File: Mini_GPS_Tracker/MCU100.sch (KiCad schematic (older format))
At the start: 12 parts

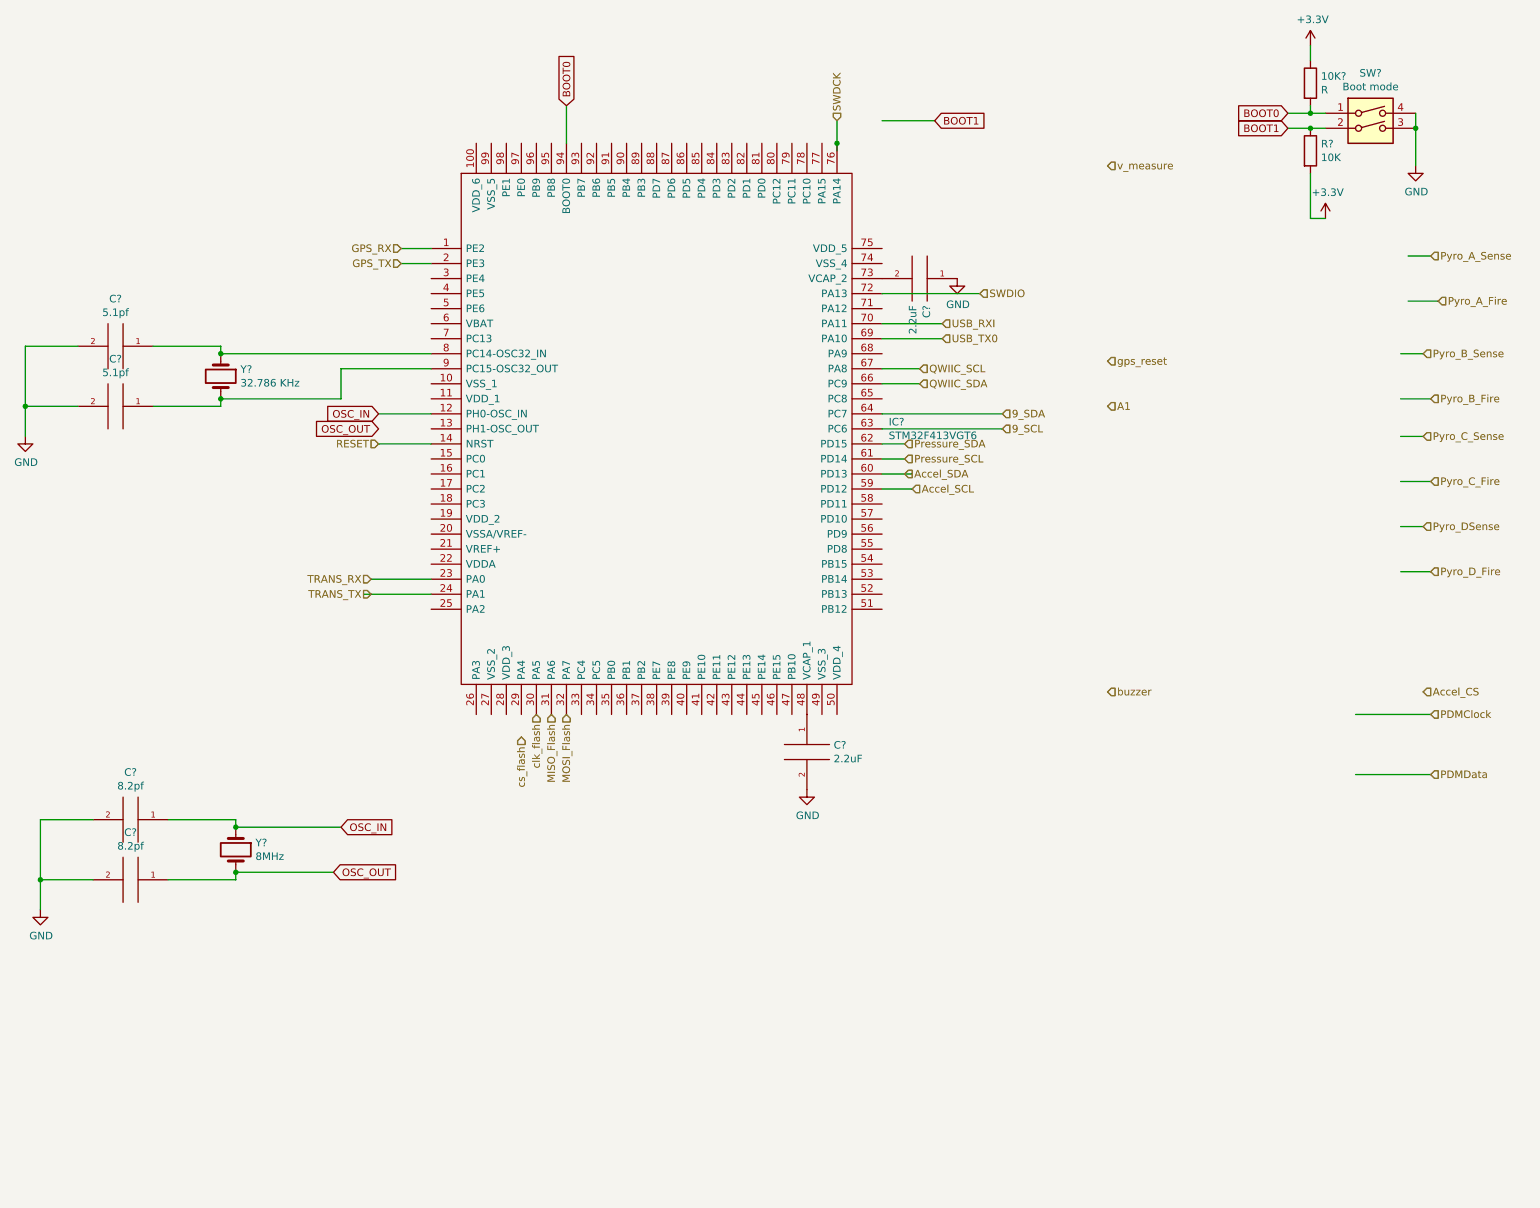
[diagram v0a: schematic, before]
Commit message: Add files via upload
Making update for 100 pin CPU
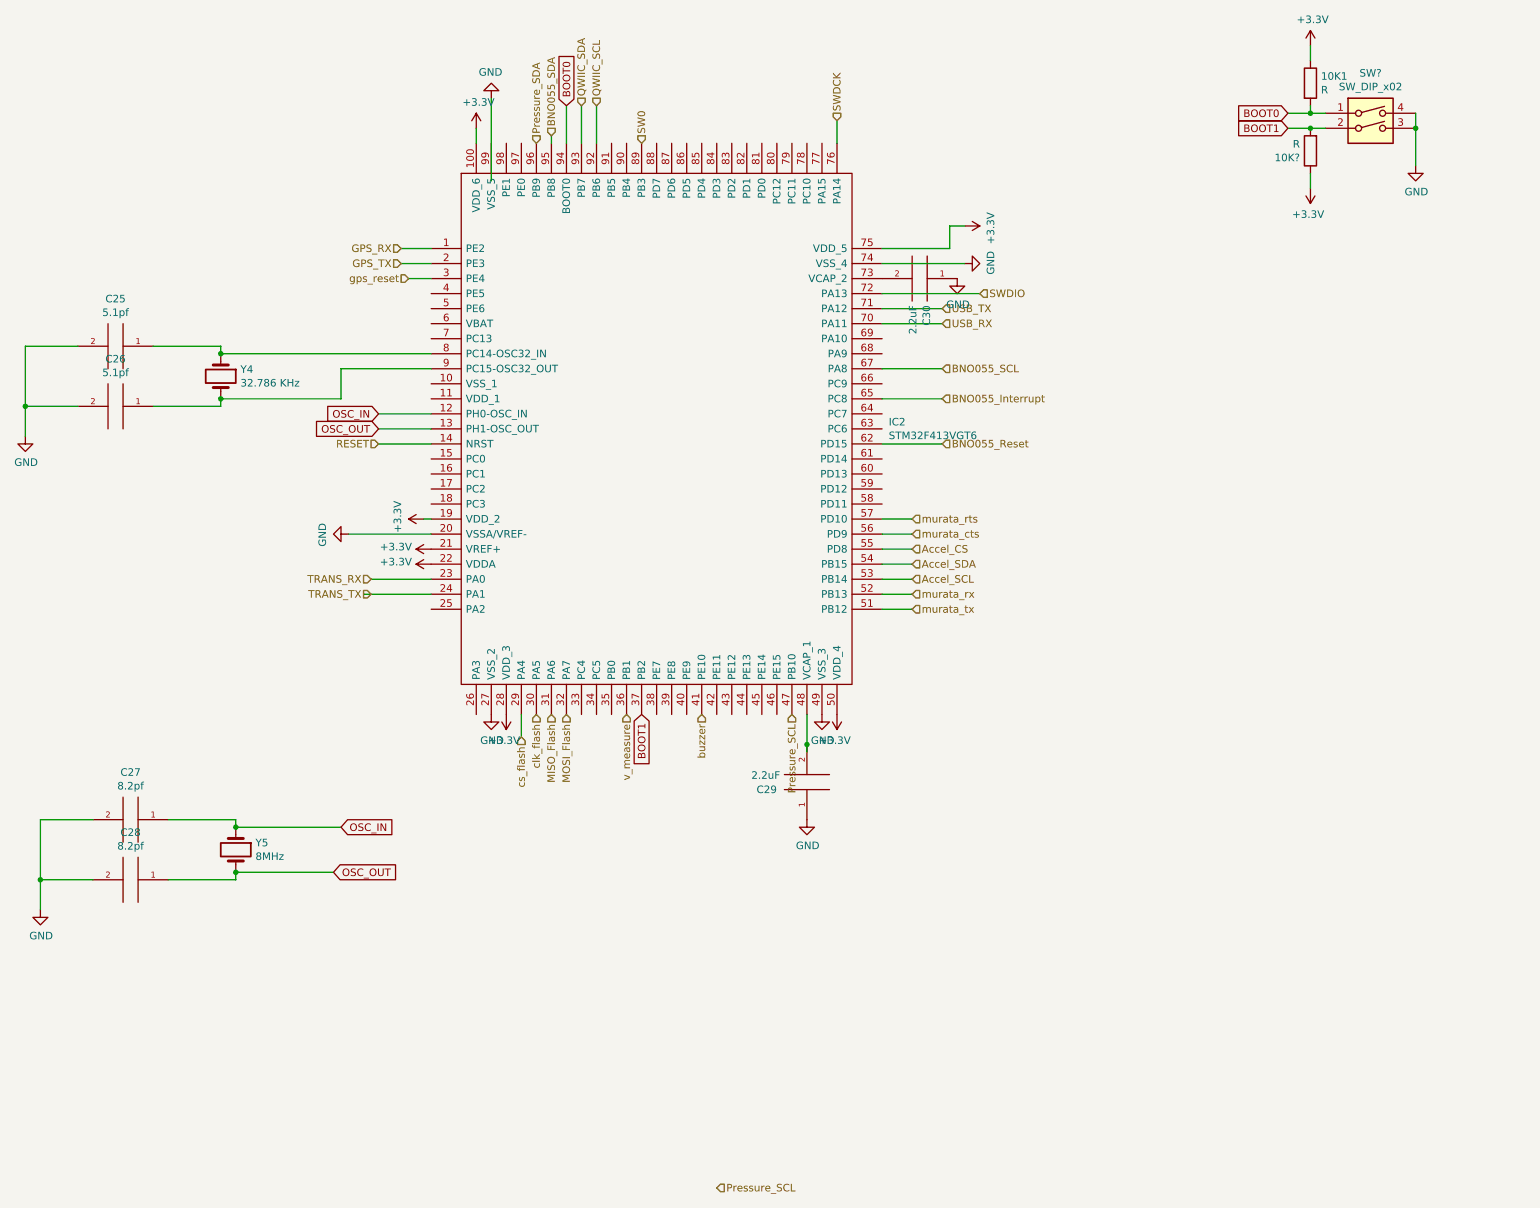
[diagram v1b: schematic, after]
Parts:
- removed R?: 10K, symbol Device:R
- removed SW?: Boot mode, symbol Switch:SW_DIP_x02
- added 10K?: R, symbol Device:R
- added SW?: SW_DIP_x02, symbol Switch:SW_DIP_x02
- gave numbers to parts that had none: 10
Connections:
- net labels added: BNO055_Interrupt, BNO055_Reset, BNO055_SCL, BNO055_SDA, SW0, USB_RX, USB_TX, murata_cts, murata_rts, murata_rx, murata_tx
- net labels removed: 9_SCL, 9_SDA, A1, PDMClock, PDMData, Pyro_A_Fire, Pyro_A_Sense, Pyro_B_Fire, Pyro_B_Sense, Pyro_C_Fire, Pyro_C_Sense, Pyro_DSense, Pyro_D_Fire, USB_RXI, USB_TX0
- wire segments 63 -> 68
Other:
- moved on the sheet: C29

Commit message: Add files via upload
Splitting board into modules
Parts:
- gave numbers to parts that had none: 2
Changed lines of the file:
@@
 $Descr A4 11693 8268
 encoding utf-8
-Sheet 7 7
+Sheet 7 13
 Title ""
 Date ""
@@
 P 9550 1950
 AR Path="/5E9FE63A/5EAF1BAE" Ref="10K?"  Part="1"
-AR Path="/5EA0B5A0/5EAF1BAE" Ref="10K?"  Part="1"
-F 0 "10K?" H 9620 1996 50  0000 L CNN
+AR Path="/5EA0B5A0/5EAF1BAE" Ref="10K2"  Part="1"
+F 0 "10K2" H 9620 1996 50  0000 L CNN
 F 1 "R" H 9620 1905 50  0000 L CNN
 F 2 "" V 9480 1950 50  0001 C CNN
@@
 P 9550 2200
 AR Path="/5E9FE63A/5EAF1BB4" Ref="#PWR?"  Part="1"
-AR Path="/5EA0B5A0/5EAF1BB4" Ref="#PWR?"  Part="1"
-F 0 "#PWR?" H 9550 2050 50  0001 C CNN
+AR Path="/5EA0B5A0/5EAF1BB4" Ref="#PWR044"  Part="1"
+F 0 "#PWR044" H 9550 2050 50  0001 C CNN
 F 1 "+3.3V" H 9565 2373 50  0000 C CNN
 F 2 "" H 9550 2200 50  0001 C CNN
@@
 	9550 2100 9550 2200
 $Comp
-L Switch:SW_DIP_x02 SW?
+L Switch:SW_DIP_x02 SW3
 U 1 1 5EAF28CC
 P 9950 1800
-F 0 "SW?" H 9950 2167 50  0000 C CNN
+F 0 "SW3" H 9950 2167 50  0000 C CNN
 F 1 "SW_DIP_x02" H 9950 2076 50  0000 C CNN
 F 2 "" H 9950 1800 50  0001 C CNN
@@
 	3550 2800 3700 2800
 $Comp
-L power:+3.3V #PWR?
+L power:+3.3V #PWR041
 U 1 1 5EB19606
 P 6400 5700
-F 0 "#PWR?" H 6400 5550 50  0001 C CNN
+F 0 "#PWR041" H 6400 5550 50  0001 C CNN
 F 1 "+3.3V" H 6415 5873 50  0000 C CNN
 F 2 "" H 6400 5700 50  0001 C CNN
@@
 $EndComp
 $Comp
-L power:GND #PWR?
+L power:GND #PWR034
 U 1 1 5EB1A30A
 P 4100 5700
-F 0 "#PWR?" H 4100 5450 50  0001 C CNN
+F 0 "#PWR034" H 4100 5450 50  0001 C CNN
 F 1 "GND" H 4105 5527 50  0000 C CNN
 F 2 "" H 4100 5700 50  0001 C CNN
@@
 $EndComp
 $Comp
-L power:+3.3V #PWR?
+L power:+3.3V #PWR036
 U 1 1 5EB1A310
 P 4200 5700
-F 0 "#PWR?" H 4200 5550 50  0001 C CNN
+F 0 "#PWR036" H 4200 5550 50  0001 C CNN
 F 1 "+3.3V" H 4215 5873 50  0000 C CNN
 F 2 "" H 4200 5700 50  0001 C CNN
@@
 $EndComp
 $Comp
-L power:GND #PWR?
+L power:GND #PWR043
 U 1 1 5EB1FB89
 P 7250 2700
-F 0 "#PWR?" H 7250 2450 50  0001 C CNN
+F 0 "#PWR043" H 7250 2450 50  0001 C CNN
 F 1 "GND" H 7255 2527 50  0000 C CNN
 F 2 "" H 7250 2700 50  0001 C CNN
@@
 $EndComp
 $Comp
-L power:+3.3V #PWR?
+L power:+3.3V #PWR042
 U 1 1 5EB1FB8F
 P 7250 2450
-F 0 "#PWR?" H 7250 2300 50  0001 C CNN
+F 0 "#PWR042" H 7250 2300 50  0001 C CNN
 F 1 "+3.3V" H 7265 2623 50  0000 C CNN
 F 2 "" H 7250 2450 50  0001 C CNN
@@
 	7150 2450 7250 2450
 $Comp
-L power:GND #PWR?
+L power:GND #PWR033
 U 1 1 5EB279CF
 P 4100 1600
-F 0 "#PWR?" H 4100 1350 50  0001 C CNN
+F 0 "#PWR033" H 4100 1350 50  0001 C CNN
 F 1 "GND" H 4105 1427 50  0000 C CNN
 F 2 "" H 4100 1600 50  0001 C CNN
@@
 $EndComp
 $Comp
-L power:+3.3V #PWR?
+L power:+3.3V #PWR032
 U 1 1 5EB279D5
 P 4000 1800
-F 0 "#PWR?" H 4000 1650 50  0001 C CNN
+F 0 "#PWR032" H 4000 1650 50  0001 C CNN
 F 1 "+3.3V" H 4015 1973 50  0000 C CNN
 F 2 "" H 4000 1800 50  0001 C CNN
@@
 	6200 5700 6200 5900
 $Comp
-L power:GND #PWR?
+L power:GND #PWR039
 U 1 1 5EB2B596
 P 6200 6400
-F 0 "#PWR?" H 6200 6150 50  0001 C CNN
+F 0 "#PWR039" H 6200 6150 50  0001 C CNN
 F 1 "GND" H 6205 6227 50  0000 C CNN
 F 2 "" H 6200 6400 50  0001 C CNN
@@
 	6700 4400 6900 4400
 $Comp
-L power:GND #PWR?
+L power:GND #PWR014
 U 1 1 5EB5E14F
 P 3150 4500
-F 0 "#PWR?" H 3150 4250 50  0001 C CNN
+F 0 "#PWR014" H 3150 4250 50  0001 C CNN
 F 1 "GND" H 3155 4327 50  0000 C CNN
 F 2 "" H 3150 4500 50  0001 C CNN
@@
 $EndComp
 $Comp
-L power:+3.3V #PWR?
+L power:+3.3V #PWR015
 U 1 1 5EB5E155
 P 3650 4400
-F 0 "#PWR?" H 3650 4250 50  0001 C CNN
+F 0 "#PWR015" H 3650 4250 50  0001 C CNN
 F 1 "+3.3V" H 3665 4573 50  0000 C CNN
 F 2 "" H 3650 4400 50  0001 C CNN
@@
 	3700 4400 3650 4400
 $Comp
-L power:+3.3V #PWR?
+L power:+3.3V #PWR017
 U 1 1 5EB62623
 P 3700 4700
-F 0 "#PWR?" H 3700 4550 50  0001 C CNN
+F 0 "#PWR017" H 3700 4550 50  0001 C CNN
 F 1 "+3.3V" V 3715 4828 50  0000 L CNN
 F 2 "" H 3700 4700 50  0001 C CNN
@@
 $EndComp
 $Comp
-L power:+3.3V #PWR?
+L power:+3.3V #PWR016
 U 1 1 5EB62F7B
 P 3700 4600
-F 0 "#PWR?" H 3700 4450 50  0001 C CNN
+F 0 "#PWR016" H 3700 4450 50  0001 C CNN
 F 1 "+3.3V" V 3715 4728 50  0000 L CNN
 F 2 "" H 3700 4600 50  0001 C CNN
